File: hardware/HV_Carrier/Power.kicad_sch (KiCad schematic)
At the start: 12 parts, among them J8 USB_C_Receptacle_USB2.0_16P

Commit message: updatred PP
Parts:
- removed TP10: PP OV, TestPoint:TestPoint_THTPad_D3.0mm_Drill1.5mm, symbol Connector:TestPoint
- removed TP11: PP SOURCE, TestPoint:TestPoint_THTPad_D3.0mm_Drill1.5mm, symbol Connector:TestPoint
- removed TP8: PP GATE, TestPoint:TestPoint_THTPad_D3.0mm_Drill1.5mm, symbol Connector:TestPoint
- removed TP9: PP EN, TestPoint:TestPoint_THTPad_D3.0mm_Drill1.5mm, symbol Connector:TestPoint
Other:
- sheet PowerProtection ports: added none; removed EN/UVLO, OV, gate, source

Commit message: update dPN for a bunch of stuff
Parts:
- removed C40: 10uF, Capacitor_SMD:C_0805_2012Metric, symbol Device:C
- removed D11: D_Schottky, Diode_SMD:D_SOD-123, symbol Device:D_Schottky
- removed D12: TPD2EUSB30DRTR, LHRS_ICs:TPD2EUSB30DRTR, symbol lhrs_ics:TPD2EUSB30DRTR
- removed J8: USB_C_Receptacle_USB2.0_16P, LHRS_Connectors:USB_C_Receptacle_GCT_USB4105-xx-A_16P_TopMnt_Horizontal, symbol lhrs_connectors:USB_C_Receptacle_USB2.0_16P
- removed R32, R33: 5.1k, Resistor_SMD:R_0603_1608Metric_Pad0.98x0.95mm_HandSolder, symbol Device:R
- added TP8: CC2, TestPoint:TestPoint_THTPad_D3.0mm_Drill1.5mm, symbol Connector:TestPoint
- TP7: value USB_5V -> CC1
- renumbered TP12 to TP9
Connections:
- net USB_5V renamed USB-C Connector/CC1
- new net USB-C Connector/CC2: TP8.1
- no-connect marks 2 -> 0
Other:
- added sheet USB-C Connector (USB-C Connector.kicad_sch)
- note removed: "5.5V working 7V breakdown 8V clamping"
- note removed: "Pulldowns for 5V USB-C PD"
- note removed: "USB Protection"
- note removed: "USB-C Port"

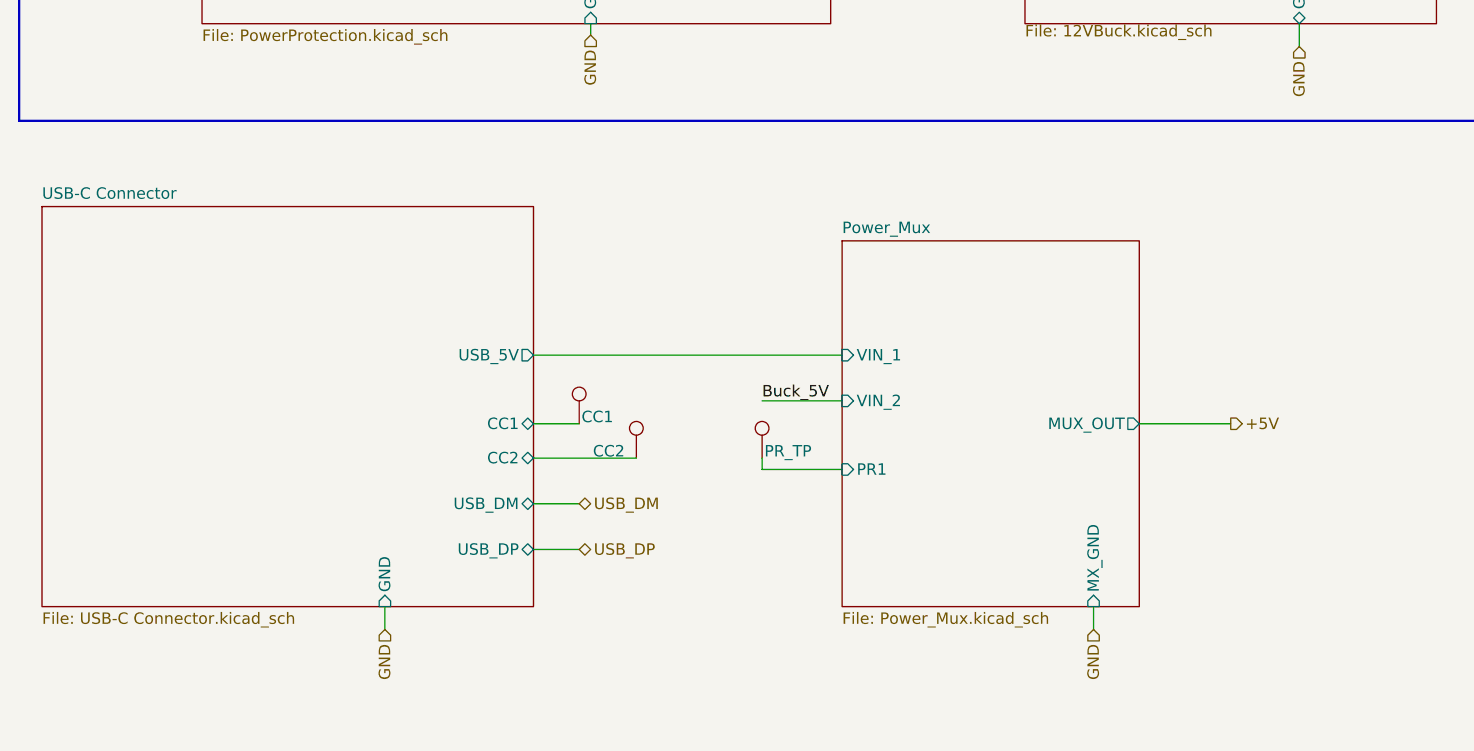
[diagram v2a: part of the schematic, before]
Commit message: added scrut breakout conn
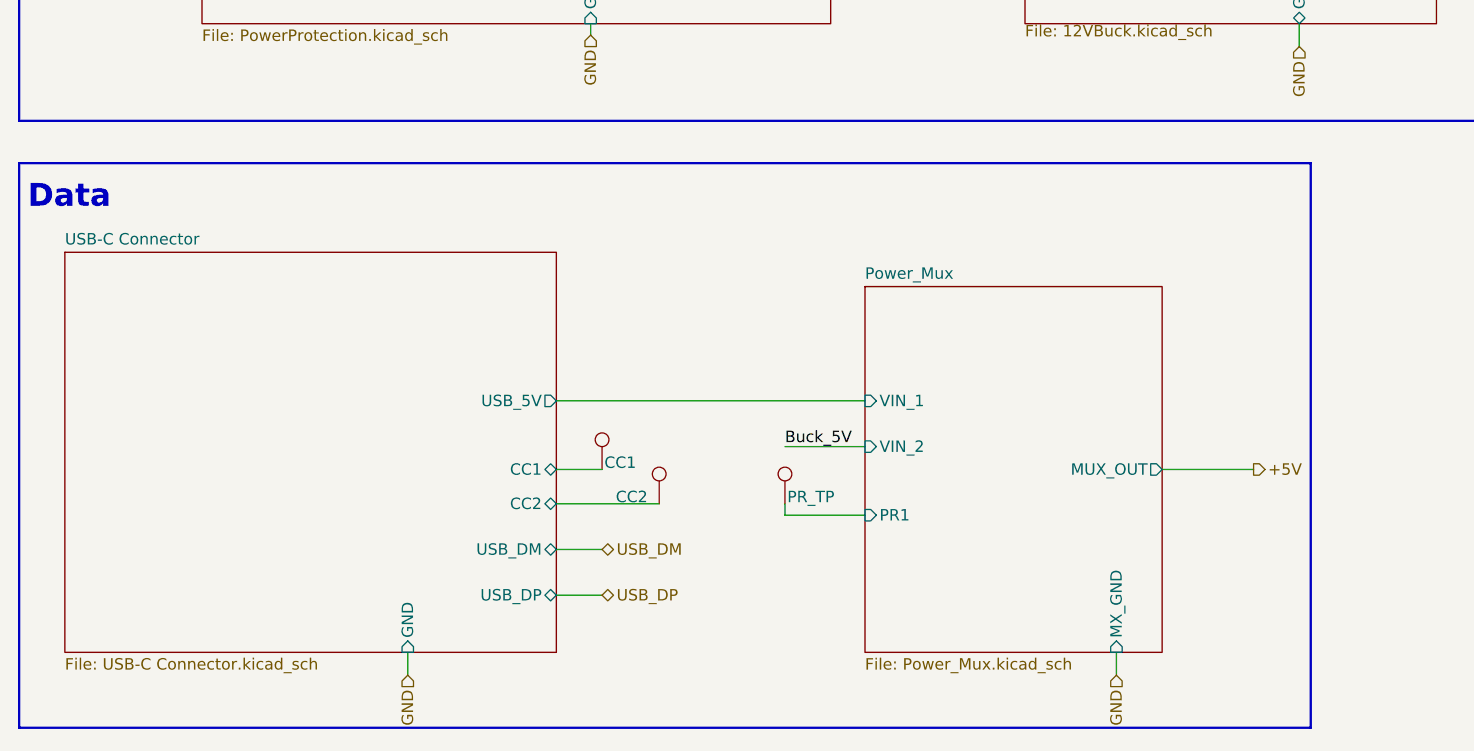
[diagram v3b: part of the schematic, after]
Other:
- note added: "Data"
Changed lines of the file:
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@@
 	(paper "A4")
+	(rectangle
+		(start 19.05 77.724)
+		(end 162.56 140.462)
+		(stroke
+			(width 0.254)
+			(type solid)
+		)
+		(fill
+			(type none)
+		)
+	)
 	(rectangle
 		(start 19.05 18.415)
@@
 		(fill
 			(type none)
+		)
+	)
+	(text "Data"
+		(exclude_from_sim no)
+		(at 24.638 81.534 0)
+		(effects
+			(font
+				(size 2.54 2.54)
+				(thickness 0.508)
+				(bold yes)
+			)
 		)
 	)
@@
 	(wire
 		(pts
-			(xy 76.2 115.57) (xy 81.28 115.57)
+			(xy 78.74 120.65) (xy 83.82 120.65)
 		)
 		(stroke
@@
 	(wire
 		(pts
-			(xy 76.2 106.68) (xy 81.28 106.68)
-		)
-		(stroke
-			(width 0)
-			(type default)
-		)
-	)
-	(wire
-		(pts
-			(xy 76.2 110.49) (xy 87.63 110.49)
+			(xy 78.74 111.76) (xy 83.82 111.76)
+		)
+		(stroke
+			(width 0)
+			(type default)
+		)
+	)
+	(wire
+		(pts
+			(xy 78.74 115.57) (xy 90.17 115.57)
 		)
 		(stroke
@@
 	(wire
 		(pts
-			(xy 59.69 129.54) (xy 59.69 127)
+			(xy 62.23 134.62) (xy 62.23 132.08)
 		)
 		(stroke
@@
 	(wire
 		(pts
-			(xy 110.49 111.76) (xy 101.6 111.76)
+			(xy 113.03 116.84) (xy 104.14 116.84)
 		)
 		(stroke
@@
 	(wire
 		(pts
-			(xy 101.6 104.14) (xy 110.49 104.14)
-		)
-		(stroke
-			(width 0)
-			(type default)
-		)
-	)
-	(wire
-		(pts
-			(xy 76.2 120.65) (xy 81.28 120.65)
-		)
-		(stroke
-			(width 0)
-			(type default)
-		)
-	)
-	(wire
-		(pts
-			(xy 143.51 106.68) (xy 153.67 106.68)
-		)
-		(stroke
-			(width 0)
-			(type default)
-		)
-	)
-	(wire
-		(pts
-			(xy 101.6 110.49) (xy 101.6 111.76)
-		)
-		(stroke
-			(width 0)
-			(type default)
-		)
-	)
-	(wire
-		(pts
-			(xy 76.2 99.06) (xy 110.49 99.06)
-		)
-		(stroke
-			(width 0)
-			(type default)
-		)
-	)
-	(wire
-		(pts
-			(xy 138.43 129.54) (xy 138.43 127)
+			(xy 104.14 109.22) (xy 113.03 109.22)
+		)
+		(stroke
+			(width 0)
+			(type default)
+		)
+	)
+	(wire
+		(pts
+			(xy 78.74 125.73) (xy 83.82 125.73)
+		)
+		(stroke
+			(width 0)
+			(type default)
+		)
+	)
+	(wire
+		(pts
+			(xy 146.05 111.76) (xy 156.21 111.76)
+		)
+		(stroke
+			(width 0)
+			(type default)
+		)
+	)
+	(wire
+		(pts
+			(xy 104.14 115.57) (xy 104.14 116.84)
+		)
+		(stroke
+			(width 0)
+			(type default)
+		)
+	)
+	(wire
+		(pts
+			(xy 78.74 104.14) (xy 113.03 104.14)
+		)
+		(stroke
+			(width 0)
+			(type default)
+		)
+	)
+	(wire
+		(pts
+			(xy 140.97 134.62) (xy 140.97 132.08)
 		)
 		(stroke
@@
 	)
 	(label "Buck_5V"
-		(at 101.6 104.14 0)
+		(at 104.14 109.22 0)
 		(effects
 			(font
@@
 	(hierarchical_label "USB_DP"
 		(shape bidirectional)
-		(at 81.28 120.65 0)
+		(at 83.82 125.73 0)
 		(effects
 			(font
@@
 	(hierarchical_label "USB_DM"
 		(shape bidirectional)
-		(at 81.28 115.57 0)
+		(at 83.82 120.65 0)
 		(effects
 			(font
@@
 	(hierarchical_label "+5V"
 		(shape output)
-		(at 153.67 106.68 0)
+		(at 156.21 111.76 0)
 		(effects
 			(font
@@
 	(hierarchical_label "GND"
 		(shape input)
-		(at 59.69 129.54 270)
+		(at 62.23 134.62 270)
 		(effects
 			(font
@@
 	(hierarchical_label "GND"
 		(shape input)
-		(at 138.43 129.54 270)
+		(at 140.97 134.62 270)
 		(effects
 			(font
@@
 	(symbol
 		(lib_id "Connector:TestPoint")
-		(at 87.63 110.49 0)
+		(at 90.17 115.57 0)
 		(mirror y)
 		(unit 1)
@@
 		(dnp no)
 		(property "Reference" "TP8"
-			(at 85.09 105.9179 0)
+			(at 87.63 110.9979 0)
 			(hide yes)
 			(show_name no)
@@
 		)
 		(property "Value" "CC2"
-			(at 82.804 109.728 0)
+			(at 85.344 114.808 0)
 			(show_name no)
 			(do_not_autoplace no)
@@
 		)
 		(property "Footprint" "TestPoint:TestPoint_THTPad_D3.0mm_Drill1.5mm"
-			(at 82.55 110.49 0)
+			(at 85.09 115.57 0)
 			(hide yes)
 			(show_name no)
@@
 		)
 		(property "Datasheet" ""
-			(at 82.55 110.49 0)
+			(at 85.09 115.57 0)
 			(hide yes)
 			(show_name no)
@@
 		)
 		(property "Description" "test point"
-			(at 87.63 110.49 0)
+			(at 90.17 115.57 0)
 			(hide yes)
 			(show_name no)
@@
 	(symbol
 		(lib_id "Connector:TestPoint")
-		(at 101.6 110.49 0)
+		(at 104.14 115.57 0)
 		(mirror y)
 		(unit 1)
@@
 		(dnp no)
 		(property "Reference" "TP9"
-			(at 99.06 105.9179 0)
+			(at 101.6 110.9979 0)
 			(hide yes)
 			(show_name no)
@@
 		)
 		(property "Value" "PR_TP"
-			(at 101.854 109.728 0)
+			(at 104.394 114.808 0)
 			(show_name no)
 			(do_not_autoplace no)
@@
 		)
 		(property "Footprint" "TestPoint:TestPoint_THTPad_D3.0mm_Drill1.5mm"
-			(at 96.52 110.49 0)
+			(at 99.06 115.57 0)
 			(hide yes)
 			(show_name no)
@@
 		)
 		(property "Datasheet" ""
-			(at 96.52 110.49 0)
+			(at 99.06 115.57 0)
 			(hide yes)
 			(show_name no)
@@
 		)
 		(property "Description" "test point"
-			(at 101.6 110.49 0)
+			(at 104.14 115.57 0)
 			(hide yes)
 			(show_name no)
@@
 	(symbol
 		(lib_id "Connector:TestPoint")
-		(at 81.28 106.68 0)
+		(at 83.82 111.76 0)
 		(mirror y)
 		(unit 1)
@@
 		(dnp no)
 		(property "Reference" "TP7"
-			(at 78.74 102.1079 0)
+			(at 81.28 107.1879 0)
 			(hide yes)
 			(show_name no)
@@
 		)
 		(property "Value" "CC1"
-			(at 81.534 105.918 0)
+			(at 84.074 110.998 0)
 			(show_name no)
 			(do_not_autoplace no)
@@
 		)
 		(property "Footprint" "TestPoint:TestPoint_THTPad_D3.0mm_Drill1.5mm"
-			(at 76.2 106.68 0)
+			(at 78.74 111.76 0)
 			(hide yes)
 			(show_name no)
@@
 		)
 		(property "Datasheet" ""
-			(at 76.2 106.68 0)
+			(at 78.74 111.76 0)
 			(hide yes)
 			(show_name no)
@@
 		)
 		(property "Description" "test point"
-			(at 81.28 106.68 0)
+			(at 83.82 111.76 0)
 			(hide yes)
 			(show_name no)
@@
 	)
 	(sheet
-		(at 21.59 82.55)
+		(at 24.13 87.63)
 		(size 54.61 44.45)
 		(exclude_from_sim no)
@@
 		)
 		(property "Sheetname" "USB-C Connector"
-			(at 21.59 81.8384 0)
+			(at 24.13 86.9184 0)
 			(show_name no)
 			(do_not_autoplace no)
@@
 		)
 		(property "Sheetfile" "USB-C Connector.kicad_sch"
-			(at 21.59 127.5846 0)
+			(at 24.13 132.6646 0)
 			(show_name no)
 			(do_not_autoplace no)
@@
 		)
 		(property "Author" "Shuopu Wang"
-			(at 0 0.254 0)
+			(at 2.54 5.334 0)
 			(hide yes)
 			(show_name no)
@@
 		)
 		(property "Date Modified" "9/5/2026"
-			(at 0 0.254 0)
+			(at 2.54 5.334 0)
 			(hide yes)
 			(show_name no)
@@
 		)
 		(pin "CC1" bidirectional
-			(at 76.2 106.68 0)
+			(at 78.74 111.76 0)
 			(effects
 				(font
@@
 		)
 		(pin "CC2" bidirectional
-			(at 76.2 110.49 0)
+			(at 78.74 115.57 0)
 			(effects
 				(font
@@
 		)
 		(pin "GND" input
-			(at 59.69 127 270)
+			(at 62.23 132.08 270)
 			(effects
 				(font
@@
 		)
 		(pin "USB_5V" output
-			(at 76.2 99.06 0)
+			(at 78.74 104.14 0)
 			(effects
 				(font
@@
 		)
 		(pin "USB_DM" bidirectional
-			(at 76.2 115.57 0)
+			(at 78.74 120.65 0)
 			(effects
 				(font
@@
 		)
 		(pin "USB_DP" bidirectional
-			(at 76.2 120.65 0)
+			(at 78.74 125.73 0)
 			(effects
 				(font
@@
 	)
 	(sheet
-		(at 110.49 86.36)
+		(at 113.03 91.44)
 		(size 33.02 40.64)
 		(exclude_from_sim no)
@@
 		)
 		(property "Sheetname" "Power_Mux"
-			(at 110.49 85.6484 0)
+			(at 113.03 90.7284 0)
 			(show_name no)
 			(do_not_autoplace no)
@@
 		)
 		(property "Sheetfile" "Power_Mux.kicad_sch"
-			(at 110.49 127.5846 0)
+			(at 113.03 132.6646 0)
 			(show_name no)
 			(do_not_autoplace no)
@@
 		)
 		(pin "MUX_OUT" output
-			(at 143.51 106.68 0)
+			(at 146.05 111.76 0)
 			(effects
 				(font
@@
 		)
 		(pin "MX_GND" input
-			(at 138.43 127 270)
+			(at 140.97 132.08 270)
 			(effects
 				(font
@@
 		)
 		(pin "PR1" input
-			(at 110.49 111.76 180)
+			(at 113.03 116.84 180)
 			(effects
 				(font
@@
 		)
 		(pin "VIN_1" input
-			(at 110.49 99.06 180)
+			(at 113.03 104.14 180)
 			(effects
 				(font
@@
 		)
 		(pin "VIN_2" input
-			(at 110.49 104.14 180)
-			(effects
-				(font
+			(at 113.03 109.22 180)
+			(effects
+				(font
